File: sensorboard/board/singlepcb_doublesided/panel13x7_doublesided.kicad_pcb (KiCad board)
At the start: 2 copper layers, 200 x 287 mm, 182 parts, among them U0A SiPM, U0B SiPM, U0C SiPM, U0D SiPM, U0E SiPM, U0F SiPM, U0G SiPM, U10A SiPM, U10B SiPM, U10C SiPM, U10D SiPM, U10E SiPM, U10F SiPM, U10G SiPM, U11A SiPM, U11B SiPM, U11C SiPM, U11D SiPM, U11E SiPM, U11F SiPM, U11G SiPM, U12A SiPM, U12B SiPM, U12C SiPM, U12D SiPM, U12E SiPM, U12F SiPM, U12G SiPM, U1A SiPM, U1B SiPM, U1C SiPM, U1D SiPM, U1E SiPM, U1F SiPM, U1G SiPM, U2A SiPM, U2B SiPM, U2C SiPM, U2D SiPM, U2E SiPM, U2F SiPM, U2G SiPM, U3A SiPM, U3B SiPM, U3C SiPM, U3D SiPM, U3E SiPM, U3F SiPM, U3G SiPM, U4A SiPM, U4B SiPM, U4C SiPM, U4D SiPM, U4E SiPM, U4F SiPM, U4G SiPM, U5A SiPM, U5B SiPM, U5C SiPM, U5D SiPM, U5E SiPM, U5F SiPM, U5G SiPM, U6A SiPM, U6B SiPM, U6C SiPM, U6D SiPM, U6E SiPM, U6F SiPM, U6G SiPM, U7A SiPM, U7B SiPM, U7C SiPM, U7D SiPM, U7E SiPM, U7F SiPM, U7G SiPM, U8A SiPM, U8B SiPM, U8C SiPM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

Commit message: Updated 13x7 panel for review.
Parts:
- removed S0A, S0B, S0C, S0D, S0E, S0F: IDC4, idc4:idc4
- removed the S1A at (55.7, 50.7)
- removed U0B, U0C, U0D, U0E, U0F, U0G: SiPM, sipm:sipm
- removed the U1A at (55.6, 29.5)
- added S13A: IDC4, idc4:idc4, B.Cu at (172.3, 50.7)
- added S13B: IDC4, idc4:idc4, B.Cu at (172.3, 81.2)
- added S13C: IDC4, idc4:idc4, B.Cu at (172.3, 111.7)
- added S13D: IDC4, idc4:idc4, B.Cu at (172.3, 142.2)
- added S13E: IDC4, idc4:idc4, B.Cu at (172.3, 172.7)
- added S13F: IDC4, idc4:idc4, B.Cu at (172.3, 203.2)
- added S13G: IDC4, idc4:idc4, B.Cu at (172.3, 233.7)
- added U13A: SiPM, sipm:sipm, F.Cu at (172.2, 29.5)
- added U13B: SiPM, sipm:sipm, F.Cu at (172.2, 60.0)
- added U13C: SiPM, sipm:sipm, F.Cu at (172.2, 90.5)
- added U13D: SiPM, sipm:sipm, F.Cu at (172.2, 121.0)
- added U13E: SiPM, sipm:sipm, F.Cu at (172.2, 151.5)
- added U13F: SiPM, sipm:sipm, F.Cu at (172.2, 182.0)
- added U13G: SiPM, sipm:sipm, F.Cu at (172.2, 212.5)
- moved S4A 10.6 mm to (76.9, 50.7)
- moved S4B 10.6 mm to (76.9, 81.2)
- moved S4C 10.6 mm to (76.9, 111.7)
- moved S4D 10.6 mm to (76.9, 142.2)
- moved S4E 10.6 mm to (76.9, 172.7)
- moved S4F 10.6 mm to (76.9, 203.2)
- moved S4G 10.6 mm to (76.9, 233.7)
- moved S7A 10.6 mm to (108.7, 50.7)
- moved S7B 10.6 mm to (108.7, 81.2)
- moved S7C 10.6 mm to (108.7, 111.7)
- moved S7D 10.6 mm to (108.7, 142.2)
- moved S7E 10.6 mm to (108.7, 172.7)
- moved S7F 10.6 mm to (108.7, 203.2)
- moved S7G 10.6 mm to (108.7, 233.7)
- moved S8A 10.6 mm to (119.3, 50.7)
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- renumbered S0A to S1A, U0A to U1A
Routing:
- net GND: track 0.00 -> 3217.3 mm, vias 91 -> 364
- net Net-(S1-Pad4): track 1839.8 -> 2210.8 mm
- net Net-(S1-Pad3): track 2240.2 -> 2200.7 mm
- net (no net): track 0.60 -> 0.00 mm, vias 91 -> 0
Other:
- outline, holes or cut-outs redrawn
- board text added: "REVIEW VERSION"

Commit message: Left a space between rows, bigger fiducials, larger tabs.
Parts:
- removed S10A, S10B, S10C, S10D, S10E, S10F, S10G, S11A, S11B, S11C, S11D, S11E, S11F, S11G, S12A, S12B, S12C, S12D, S12E, S12F, S12G, S13A, S13B, S13C, S13D, S13E, S13F, S13G, S1B, S1C, S1D, S1E, S1F, S1G, S2A, S2B, S2C, S2D, S2E, S2F, S2G, S3A, S3B, S3C, S3D, S3E, S3F, S3G, S4A, S4B, S4C, S4D, S4E, S4F, S4G, S5A, S5B, S5C, S5D, S5E, S5F, S5G, S6A, S6B, S6C, S6D, S6E, S6F, S6G, S7A, S7B, S7C, S7D, S7E, S7F, S7G, S8A, S8B, S8C, S8D, S8E, S8F, S8G, S9A, S9B, S9C, S9D, S9E, S9F, S9G: IDC4, idc4:idc4
- removed U10A, U10B, U10C, U10D, U10E, U10F, U10G, U11A, U11B, U11C, U11D, U11E, U11F, U11G, U12A, U12B, U12C, U12D, U12E, U12F, U12G, U13A, U13B, U13C, U13D, U13E, U13F, U13G, U1B, U1C, U1D, U1E, U1F, U1G, U2A, U2B, U2C, U2D, U2E, U2F, U2G, U3A, U3B, U3C, U3D, U3E, U3F, U3G, U4A, U4B, U4C, U4D, U4E, U4F, U4G, U5A, U5B, U5C, U5D, U5E, U5F, U5G, U6A, U6B, U6C, U6D, U6E, U6F, U6G, U7A, U7B, U7C, U7D, U7E, U7F, U7G, U8A, U8B, U8C, U8D, U8E, U8F, U8G, U9A, U9B, U9C, U9D, U9E, U9F, U9G: SiPM, sipm:sipm
- added REF**: FID_OxPhys, oxford_fiducial:FID_OxPhys, F.Cu at (20.0, 20.0)
- added REF**: FID_OxPhys, oxford_fiducial:FID_OxPhys, F.Cu at (263.8, 207.0)
- added REF**: FID_OxPhys, oxford_fiducial:FID_OxPhys, F.Cu at (272.0, 228.8)
- added REF**: FID_OxPhys, oxford_fiducial:FID_OxPhys, F.Cu at (294.8, 207.0)
- added REF**: FID_OxPhys, oxford_fiducial:FID_OxPhys, F.Cu at (18.8, 21.0)
- added REF**: FID_OxPhys, oxford_fiducial:FID_OxPhys, F.Cu at (13.2, 260.6)
- added REF**: FID_OxPhys, oxford_fiducial:FID_OxPhys, F.Cu at (188.8, 20.0)
- added REF**: FID_OxPhys, oxford_fiducial:FID_OxPhys, F.Cu at (196.4, 260.6)
- added S101: IDC4, idc4:idc4, B.Cu at (140.5, 50.7)
- added S102: IDC4, idc4:idc4, B.Cu at (140.5, 81.2)
- added S103: IDC4, idc4:idc4, B.Cu at (140.5, 111.7)
- added S104: IDC4, idc4:idc4, B.Cu at (140.5, 142.2)
- added S105: IDC4, idc4:idc4, B.Cu at (140.5, 182.7)
- added S106: IDC4, idc4:idc4, B.Cu at (140.5, 213.2)
- added S107: IDC4, idc4:idc4, B.Cu at (140.5, 243.7)
- added S111: IDC4, idc4:idc4, B.Cu at (151.1, 50.7)
- added S112: IDC4, idc4:idc4, B.Cu at (151.1, 81.2)
- added S113: IDC4, idc4:idc4, B.Cu at (151.1, 111.7)
- added S114: IDC4, idc4:idc4, B.Cu at (151.1, 142.2)
- added S115: IDC4, idc4:idc4, B.Cu at (151.1, 182.7)
- added S116: IDC4, idc4:idc4, B.Cu at (151.1, 213.2)
- added S117: IDC4, idc4:idc4, B.Cu at (151.1, 243.7)
- added S12: IDC4, idc4:idc4, B.Cu at (45.1, 81.2)
- added S121: IDC4, idc4:idc4, B.Cu at (161.7, 50.7)
- added S122: IDC4, idc4:idc4, B.Cu at (161.7, 81.2)
- added S123: IDC4, idc4:idc4, B.Cu at (161.7, 111.7)
- added S124: IDC4, idc4:idc4, B.Cu at (161.7, 142.2)
- added S125: IDC4, idc4:idc4, B.Cu at (161.7, 182.7)
- added S126: IDC4, idc4:idc4, B.Cu at (161.7, 213.2)
- added S127: IDC4, idc4:idc4, B.Cu at (161.7, 243.7)
- added S13: IDC4, idc4:idc4, B.Cu at (45.1, 111.7)
- added S131: IDC4, idc4:idc4, B.Cu at (172.3, 50.7)
- added S132: IDC4, idc4:idc4, B.Cu at (172.3, 81.2)
- added S133: IDC4, idc4:idc4, B.Cu at (172.3, 111.7)
- added S134: IDC4, idc4:idc4, B.Cu at (172.3, 142.2)
- added S135: IDC4, idc4:idc4, B.Cu at (172.3, 182.7)
- added S136: IDC4, idc4:idc4, B.Cu at (172.3, 213.2)
- added S137: IDC4, idc4:idc4, B.Cu at (172.3, 243.7)
- added S14: IDC4, idc4:idc4, B.Cu at (45.1, 142.2)
- added S15: IDC4, idc4:idc4, B.Cu at (45.1, 182.7)
- added S16: IDC4, idc4:idc4, B.Cu at (45.1, 213.2)
- added S17: IDC4, idc4:idc4, B.Cu at (45.1, 243.7)
- added S21: IDC4, idc4:idc4, B.Cu at (55.7, 50.7)
- added S22: IDC4, idc4:idc4, B.Cu at (55.7, 81.2)
- added S23: IDC4, idc4:idc4, B.Cu at (55.7, 111.7)
- added S24: IDC4, idc4:idc4, B.Cu at (55.7, 142.2)
- added S25: IDC4, idc4:idc4, B.Cu at (55.7, 182.7)
- added S26: IDC4, idc4:idc4, B.Cu at (55.7, 213.2)
- added S27: IDC4, idc4:idc4, B.Cu at (55.7, 243.7)
- added S31: IDC4, idc4:idc4, B.Cu at (66.3, 50.7)
- added S32: IDC4, idc4:idc4, B.Cu at (66.3, 81.2)
- added S33: IDC4, idc4:idc4, B.Cu at (66.3, 111.7)
- added S34: IDC4, idc4:idc4, B.Cu at (66.3, 142.2)
- added S35: IDC4, idc4:idc4, B.Cu at (66.3, 182.7)
- added S36: IDC4, idc4:idc4, B.Cu at (66.3, 213.2)
- added S37: IDC4, idc4:idc4, B.Cu at (66.3, 243.7)
- added S41: IDC4, idc4:idc4, B.Cu at (76.9, 50.7)
- added S42: IDC4, idc4:idc4, B.Cu at (76.9, 81.2)
- added S43: IDC4, idc4:idc4, B.Cu at (76.9, 111.7)
- added S44: IDC4, idc4:idc4, B.Cu at (76.9, 142.2)
- added S45: IDC4, idc4:idc4, B.Cu at (76.9, 182.7)
- added S46: IDC4, idc4:idc4, B.Cu at (76.9, 213.2)
- added S47: IDC4, idc4:idc4, B.Cu at (76.9, 243.7)
- added S51: IDC4, idc4:idc4, B.Cu at (87.5, 50.7)
- added S52: IDC4, idc4:idc4, B.Cu at (87.5, 81.2)
- added S53: IDC4, idc4:idc4, B.Cu at (87.5, 111.7)
- added S54: IDC4, idc4:idc4, B.Cu at (87.5, 142.2)
- added S55: IDC4, idc4:idc4, B.Cu at (87.5, 182.7)
- added S56: IDC4, idc4:idc4, B.Cu at (87.5, 213.2)
- added S57: IDC4, idc4:idc4, B.Cu at (87.5, 243.7)
- added S61: IDC4, idc4:idc4, B.Cu at (98.1, 50.7)
- added S62: IDC4, idc4:idc4, B.Cu at (98.1, 81.2)
- added S63: IDC4, idc4:idc4, B.Cu at (98.1, 111.7)
- added S64: IDC4, idc4:idc4, B.Cu at (98.1, 142.2)
- added S65: IDC4, idc4:idc4, B.Cu at (98.1, 182.7)
- added S66: IDC4, idc4:idc4, B.Cu at (98.1, 213.2)
- added S67: IDC4, idc4:idc4, B.Cu at (98.1, 243.7)
- added S71: IDC4, idc4:idc4, B.Cu at (108.7, 50.7)
- added S72: IDC4, idc4:idc4, B.Cu at (108.7, 81.2)
- added S73: IDC4, idc4:idc4, B.Cu at (108.7, 111.7)
- added S74: IDC4, idc4:idc4, B.Cu at (108.7, 142.2)
- added S75: IDC4, idc4:idc4, B.Cu at (108.7, 182.7)
- added S76: IDC4, idc4:idc4, B.Cu at (108.7, 213.2)
- added S77: IDC4, idc4:idc4, B.Cu at (108.7, 243.7)
- added S81: IDC4, idc4:idc4, B.Cu at (119.3, 50.7)
- added S82: IDC4, idc4:idc4, B.Cu at (119.3, 81.2)
- added S83: IDC4, idc4:idc4, B.Cu at (119.3, 111.7)
- added S84: IDC4, idc4:idc4, B.Cu at (119.3, 142.2)
- added S85: IDC4, idc4:idc4, B.Cu at (119.3, 182.7)
- added S86: IDC4, idc4:idc4, B.Cu at (119.3, 213.2)
- added S87: IDC4, idc4:idc4, B.Cu at (119.3, 243.7)
- added S91: IDC4, idc4:idc4, B.Cu at (129.9, 50.7)
- added S92: IDC4, idc4:idc4, B.Cu at (129.9, 81.2)
- added S93: IDC4, idc4:idc4, B.Cu at (129.9, 111.7)
- added S94: IDC4, idc4:idc4, B.Cu at (129.9, 142.2)
- added S95: IDC4, idc4:idc4, B.Cu at (129.9, 182.7)
- added S96: IDC4, idc4:idc4, B.Cu at (129.9, 213.2)
- added S97: IDC4, idc4:idc4, B.Cu at (129.9, 243.7)
- added U101: SiPM, sipm:sipm, F.Cu at (140.4, 29.5)
- added U102: SiPM, sipm:sipm, F.Cu at (140.4, 60.0)
- added U103: SiPM, sipm:sipm, F.Cu at (140.4, 90.5)
- added U104: SiPM, sipm:sipm, F.Cu at (140.4, 121.0)
- added U105: SiPM, sipm:sipm, F.Cu at (140.4, 161.5)
- added U106: SiPM, sipm:sipm, F.Cu at (140.4, 192.0)
- added U107: SiPM, sipm:sipm, F.Cu at (140.4, 222.5)
- added U111: SiPM, sipm:sipm, F.Cu at (151.0, 29.5)
- added U112: SiPM, sipm:sipm, F.Cu at (151.0, 60.0)
- added U113: SiPM, sipm:sipm, F.Cu at (151.0, 90.5)
- added U114: SiPM, sipm:sipm, F.Cu at (151.0, 121.0)
- added U115: SiPM, sipm:sipm, F.Cu at (151.0, 161.5)
- added U116: SiPM, sipm:sipm, F.Cu at (151.0, 192.0)
- added U117: SiPM, sipm:sipm, F.Cu at (151.0, 222.5)
- added U12: SiPM, sipm:sipm, F.Cu at (45.0, 60.0)
- added U121: SiPM, sipm:sipm, F.Cu at (161.6, 29.5)
- added U122: SiPM, sipm:sipm, F.Cu at (161.6, 60.0)
- added U123: SiPM, sipm:sipm, F.Cu at (161.6, 90.5)
- added U124: SiPM, sipm:sipm, F.Cu at (161.6, 121.0)
- added U125: SiPM, sipm:sipm, F.Cu at (161.6, 161.5)
- added U126: SiPM, sipm:sipm, F.Cu at (161.6, 192.0)
- added U127: SiPM, sipm:sipm, F.Cu at (161.6, 222.5)
- added U13: SiPM, sipm:sipm, F.Cu at (45.0, 90.5)
- added U131: SiPM, sipm:sipm, F.Cu at (172.2, 29.5)
- added U132: SiPM, sipm:sipm, F.Cu at (172.2, 60.0)
- added U133: SiPM, sipm:sipm, F.Cu at (172.2, 90.5)
- added U134: SiPM, sipm:sipm, F.Cu at (172.2, 121.0)
- added U135: SiPM, sipm:sipm, F.Cu at (172.2, 161.5)
- added U136: SiPM, sipm:sipm, F.Cu at (172.2, 192.0)
- added U137: SiPM, sipm:sipm, F.Cu at (172.2, 222.5)
- added U14: SiPM, sipm:sipm, F.Cu at (45.0, 121.0)
- added U15: SiPM, sipm:sipm, F.Cu at (45.0, 161.5)
- added U16: SiPM, sipm:sipm, F.Cu at (45.0, 192.0)
- added U17: SiPM, sipm:sipm, F.Cu at (45.0, 222.5)
- added U21: SiPM, sipm:sipm, F.Cu at (55.6, 29.5)
- added U22: SiPM, sipm:sipm, F.Cu at (55.6, 60.0)
- added U23: SiPM, sipm:sipm, F.Cu at (55.6, 90.5)
- added U24: SiPM, sipm:sipm, F.Cu at (55.6, 121.0)
- added U25: SiPM, sipm:sipm, F.Cu at (55.6, 161.5)
- added U26: SiPM, sipm:sipm, F.Cu at (55.6, 192.0)
- added U27: SiPM, sipm:sipm, F.Cu at (55.6, 222.5)
- added U31: SiPM, sipm:sipm, F.Cu at (66.2, 29.5)
- added U32: SiPM, sipm:sipm, F.Cu at (66.2, 60.0)
- added U33: SiPM, sipm:sipm, F.Cu at (66.2, 90.5)
- added U34: SiPM, sipm:sipm, F.Cu at (66.2, 121.0)
- added U35: SiPM, sipm:sipm, F.Cu at (66.2, 161.5)
- added U36: SiPM, sipm:sipm, F.Cu at (66.2, 192.0)
- added U37: SiPM, sipm:sipm, F.Cu at (66.2, 222.5)
- added U41: SiPM, sipm:sipm, F.Cu at (76.8, 29.5)
- added U42: SiPM, sipm:sipm, F.Cu at (76.8, 60.0)
- added U43: SiPM, sipm:sipm, F.Cu at (76.8, 90.5)
- added U44: SiPM, sipm:sipm, F.Cu at (76.8, 121.0)
- added U45: SiPM, sipm:sipm, F.Cu at (76.8, 161.5)
- added U46: SiPM, sipm:sipm, F.Cu at (76.8, 192.0)
- added U47: SiPM, sipm:sipm, F.Cu at (76.8, 222.5)
- added U51: SiPM, sipm:sipm, F.Cu at (87.4, 29.5)
- added U52: SiPM, sipm:sipm, F.Cu at (87.4, 60.0)
- added U53: SiPM, sipm:sipm, F.Cu at (87.4, 90.5)
- added U54: SiPM, sipm:sipm, F.Cu at (87.4, 121.0)
- added U55: SiPM, sipm:sipm, F.Cu at (87.4, 161.5)
- added U56: SiPM, sipm:sipm, F.Cu at (87.4, 192.0)
- added U57: SiPM, sipm:sipm, F.Cu at (87.4, 222.5)
- added U61: SiPM, sipm:sipm, F.Cu at (98.0, 29.5)
- added U62: SiPM, sipm:sipm, F.Cu at (98.0, 60.0)
- added U63: SiPM, sipm:sipm, F.Cu at (98.0, 90.5)
- added U64: SiPM, sipm:sipm, F.Cu at (98.0, 121.0)
- added U65: SiPM, sipm:sipm, F.Cu at (98.0, 161.5)
- added U66: SiPM, sipm:sipm, F.Cu at (98.0, 192.0)
- added U67: SiPM, sipm:sipm, F.Cu at (98.0, 222.5)
- added U71: SiPM, sipm:sipm, F.Cu at (108.6, 29.5)
- added U72: SiPM, sipm:sipm, F.Cu at (108.6, 60.0)
- added U73: SiPM, sipm:sipm, F.Cu at (108.6, 90.5)
- added U74: SiPM, sipm:sipm, F.Cu at (108.6, 121.0)
- added U75: SiPM, sipm:sipm, F.Cu at (108.6, 161.5)
- added U76: SiPM, sipm:sipm, F.Cu at (108.6, 192.0)
- added U77: SiPM, sipm:sipm, F.Cu at (108.6, 222.5)
- added U81: SiPM, sipm:sipm, F.Cu at (119.2, 29.5)
- added U82: SiPM, sipm:sipm, F.Cu at (119.2, 60.0)
- added U83: SiPM, sipm:sipm, F.Cu at (119.2, 90.5)
- added U84: SiPM, sipm:sipm, F.Cu at (119.2, 121.0)
- added U85: SiPM, sipm:sipm, F.Cu at (119.2, 161.5)
- added U86: SiPM, sipm:sipm, F.Cu at (119.2, 192.0)
- added U87: SiPM, sipm:sipm, F.Cu at (119.2, 222.5)
- added U91: SiPM, sipm:sipm, F.Cu at (129.8, 29.5)
- added U92: SiPM, sipm:sipm, F.Cu at (129.8, 60.0)
- added U93: SiPM, sipm:sipm, F.Cu at (129.8, 90.5)
- added U94: SiPM, sipm:sipm, F.Cu at (129.8, 121.0)
- added U95: SiPM, sipm:sipm, F.Cu at (129.8, 161.5)
- added U96: SiPM, sipm:sipm, F.Cu at (129.8, 192.0)
- added U97: SiPM, sipm:sipm, F.Cu at (129.8, 222.5)
- renumbered S1A to S11, U1A to U11
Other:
- board size 200 x 287 mm -> 200 x 262.1 mm
- board text added: "SoLid SiPM sensor boards. 22 Jun 16. Nick Ryder nick.ryder@physics.ox.ac.uk"
- board text removed: "REVIEW VERSION"
- board text removed: "SoLid SiPM sensor boards. 13 Jun 16. Nick Ryder nick.ryder@physics.ox.ac.uk"

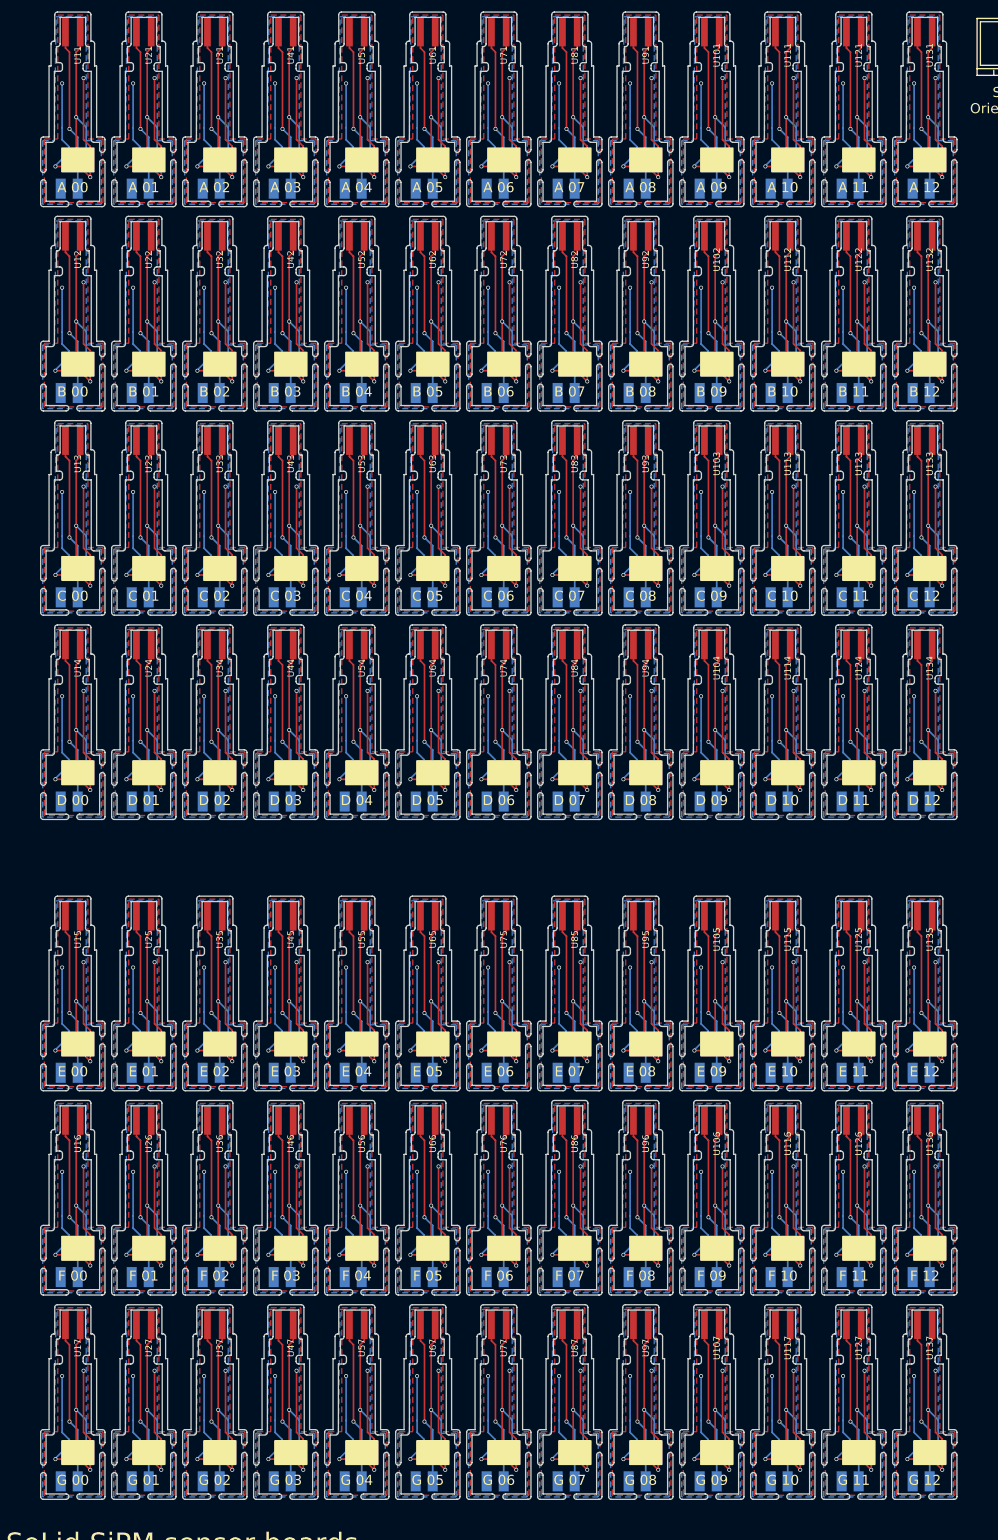
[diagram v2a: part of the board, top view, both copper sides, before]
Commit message: Working on MPPC PCB cut outs.
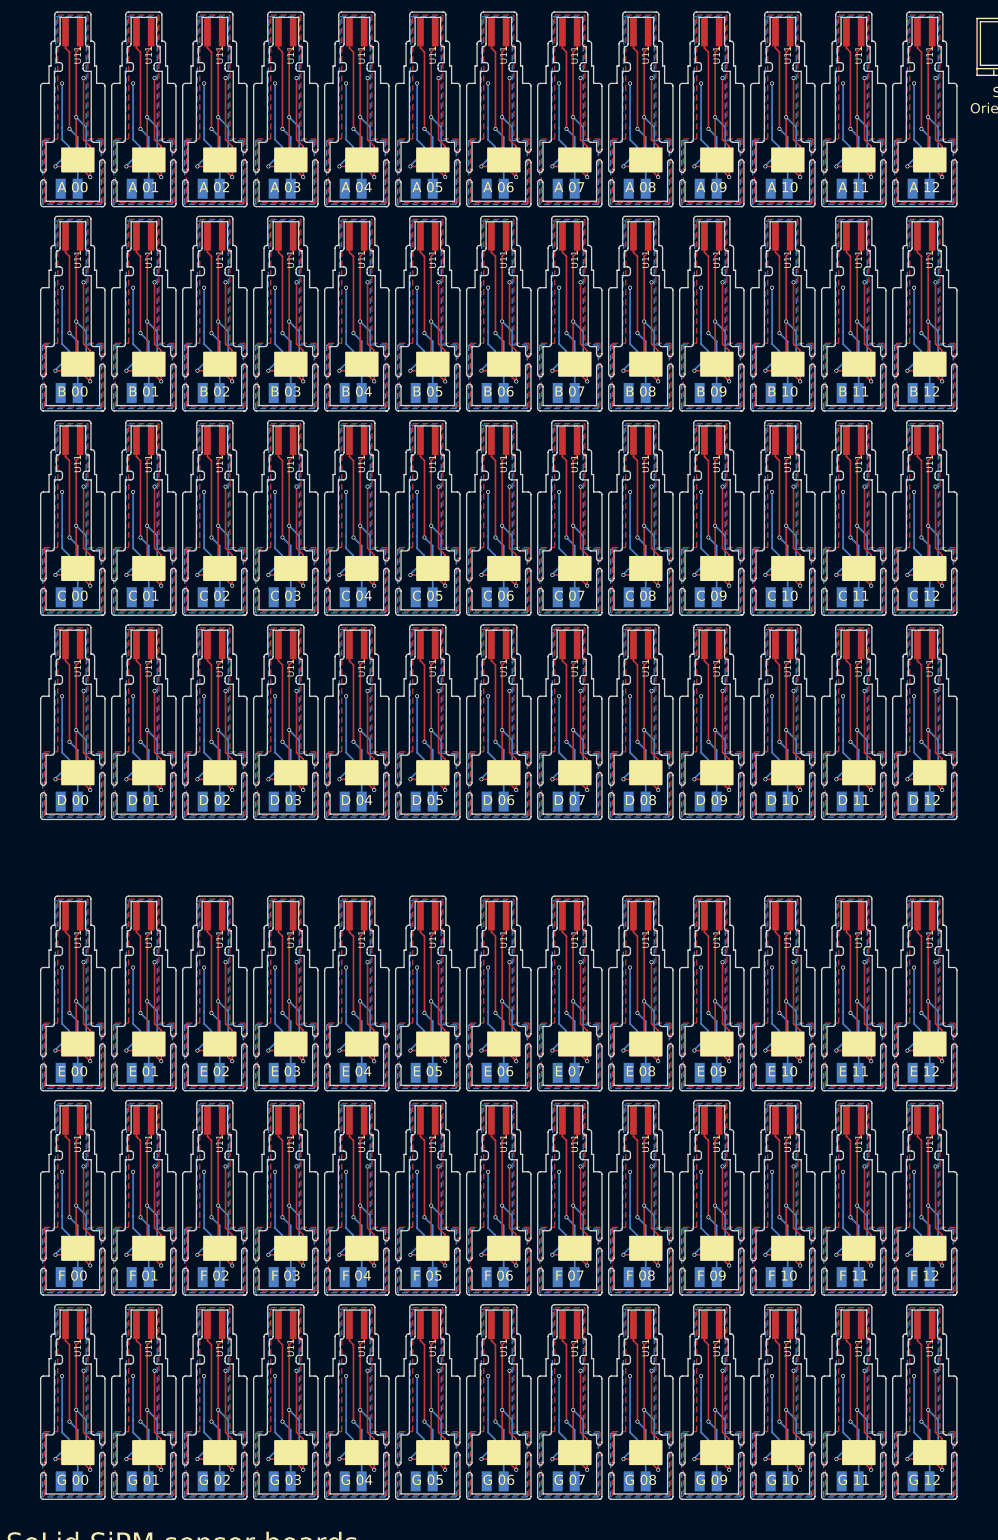
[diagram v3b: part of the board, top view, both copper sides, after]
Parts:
- removed S101, S102, S103, S104, S105, S106, S107, S111, S112, S113, S114, S115, S116, S117, S12, S121, S122, S123, S124, S125, S126, S127, S13, S131, S132, S133, S134, S135, S136, S137, S14, S15, S16, S17, S21, S22, S23, S24, S25, S26, S27, S31, S32, S33, S34, S35, S36, S37, S41, S42, S43, S44, S45, S46, S47, S51, S52, S53, S54, S55, S56, S57, S61, S62, S63, S64, S65, S66, S67, S71, S72, S73, S74, S75, S76, S77, S81, S82, S83, S84, S85, S86, S87, S91, S92, S93, S94, S95, S96, S97: IDC4, idc4:idc4
- removed U101, U102, U103, U104, U105, U106, U107, U111, U112, U113, U114, U115, U116, U117, U12, U121, U122, U123, U124, U125, U126, U127, U13, U131, U132, U133, U134, U135, U136, U137, U14, U15, U16, U17, U21, U22, U23, U24, U25, U26, U27, U31, U32, U33, U34, U35, U36, U37, U41, U42, U43, U44, U45, U46, U47, U51, U52, U53, U54, U55, U56, U57, U61, U62, U63, U64, U65, U66, U67, U71, U72, U73, U74, U75, U76, U77, U81, U82, U83, U84, U85, U86, U87, U91, U92, U93, U94, U95, U96, U97: SiPM, sipm:sipm
- added S11: IDC4, idc4:idc4, B.Cu at (87.5, 243.7)
- added S11: IDC4, idc4:idc4, B.Cu at (76.9, 213.2)
- added S11: IDC4, idc4:idc4, B.Cu at (108.7, 243.7)
- added S11: IDC4, idc4:idc4, B.Cu at (108.7, 213.2)
- added S11: IDC4, idc4:idc4, B.Cu at (98.1, 243.7)
- added S11: IDC4, idc4:idc4, B.Cu at (98.1, 213.2)
- added S11: IDC4, idc4:idc4, B.Cu at (172.3, 243.7)
- added S11: IDC4, idc4:idc4, B.Cu at (172.3, 213.2)
- added S11: IDC4, idc4:idc4, B.Cu at (119.3, 243.7)
- added S11: IDC4, idc4:idc4, B.Cu at (119.3, 213.2)
- added S11: IDC4, idc4:idc4, B.Cu at (151.1, 243.7)
- added S11: IDC4, idc4:idc4, B.Cu at (87.5, 213.2)
- added S11: IDC4, idc4:idc4, B.Cu at (151.1, 213.2)
- added S11: IDC4, idc4:idc4, B.Cu at (129.9, 243.7)
- added S11: IDC4, idc4:idc4, B.Cu at (129.9, 213.2)
- added S11: IDC4, idc4:idc4, B.Cu at (140.5, 243.7)
- added S11: IDC4, idc4:idc4, B.Cu at (140.5, 213.2)
- added S11: IDC4, idc4:idc4, B.Cu at (161.7, 243.7)
- added S11: IDC4, idc4:idc4, B.Cu at (161.7, 213.2)
- added S11: IDC4, idc4:idc4, B.Cu at (172.3, 182.7)
- added S11: IDC4, idc4:idc4, B.Cu at (161.7, 182.7)
- added S11: IDC4, idc4:idc4, B.Cu at (119.3, 182.7)
- added S11: IDC4, idc4:idc4, B.Cu at (66.3, 243.7)
- added S11: IDC4, idc4:idc4, B.Cu at (151.1, 182.7)
- added S11: IDC4, idc4:idc4, B.Cu at (129.9, 182.7)
- added S11: IDC4, idc4:idc4, B.Cu at (140.5, 182.7)
- added S11: IDC4, idc4:idc4, B.Cu at (108.7, 182.7)
- added S11: IDC4, idc4:idc4, B.Cu at (98.1, 182.7)
- added S11: IDC4, idc4:idc4, B.Cu at (87.5, 182.7)
- added S11: IDC4, idc4:idc4, B.Cu at (66.3, 182.7)
- added S11: IDC4, idc4:idc4, B.Cu at (55.7, 182.7)
- added S11: IDC4, idc4:idc4, B.Cu at (45.1, 182.7)
- added S11: IDC4, idc4:idc4, B.Cu at (76.9, 182.7)
- added S11: IDC4, idc4:idc4, B.Cu at (66.3, 213.2)
- added S11: IDC4, idc4:idc4, B.Cu at (119.3, 142.2)
- added S11: IDC4, idc4:idc4, B.Cu at (119.3, 111.7)
- added S11: IDC4, idc4:idc4, B.Cu at (119.3, 81.2)
- added S11: IDC4, idc4:idc4, B.Cu at (108.7, 142.2)
- added S11: IDC4, idc4:idc4, B.Cu at (108.7, 111.7)
- added S11: IDC4, idc4:idc4, B.Cu at (108.7, 81.2)
- added S11: IDC4, idc4:idc4, B.Cu at (98.1, 142.2)
- added S11: IDC4, idc4:idc4, B.Cu at (98.1, 111.7)
- added S11: IDC4, idc4:idc4, B.Cu at (98.1, 81.2)
- added S11: IDC4, idc4:idc4, B.Cu at (87.5, 142.2)
- added S11: IDC4, idc4:idc4, B.Cu at (55.7, 243.7)
- added S11: IDC4, idc4:idc4, B.Cu at (87.5, 111.7)
- added S11: IDC4, idc4:idc4, B.Cu at (87.5, 81.2)
- added S11: IDC4, idc4:idc4, B.Cu at (172.3, 142.2)
- added S11: IDC4, idc4:idc4, B.Cu at (172.3, 111.7)
- added S11: IDC4, idc4:idc4, B.Cu at (172.3, 81.2)
- added S11: IDC4, idc4:idc4, B.Cu at (140.5, 142.2)
- added S11: IDC4, idc4:idc4, B.Cu at (140.5, 111.7)
- added S11: IDC4, idc4:idc4, B.Cu at (140.5, 81.2)
- added S11: IDC4, idc4:idc4, B.Cu at (129.9, 142.2)
- added S11: IDC4, idc4:idc4, B.Cu at (129.9, 111.7)
- added S11: IDC4, idc4:idc4, B.Cu at (55.7, 213.2)
- added S11: IDC4, idc4:idc4, B.Cu at (129.9, 81.2)
- added S11: IDC4, idc4:idc4, B.Cu at (151.1, 142.2)
- added S11: IDC4, idc4:idc4, B.Cu at (151.1, 111.7)
- added S11: IDC4, idc4:idc4, B.Cu at (151.1, 81.2)
- added S11: IDC4, idc4:idc4, B.Cu at (161.7, 142.2)
- added S11: IDC4, idc4:idc4, B.Cu at (161.7, 111.7)
- added S11: IDC4, idc4:idc4, B.Cu at (161.7, 81.2)
- added S11: IDC4, idc4:idc4, B.Cu at (66.3, 142.2)
- added S11: IDC4, idc4:idc4, B.Cu at (66.3, 111.7)
- added S11: IDC4, idc4:idc4, B.Cu at (66.3, 81.2)
- added S11: IDC4, idc4:idc4, B.Cu at (45.1, 243.7)
- added S11: IDC4, idc4:idc4, B.Cu at (55.7, 142.2)
- added S11: IDC4, idc4:idc4, B.Cu at (55.7, 111.7)
- added S11: IDC4, idc4:idc4, B.Cu at (55.7, 81.2)
- added S11: IDC4, idc4:idc4, B.Cu at (45.1, 142.2)
- added S11: IDC4, idc4:idc4, B.Cu at (45.1, 111.7)
- added S11: IDC4, idc4:idc4, B.Cu at (45.1, 81.2)
- added S11: IDC4, idc4:idc4, B.Cu at (76.9, 142.2)
- added S11: IDC4, idc4:idc4, B.Cu at (76.9, 111.7)
- added S11: IDC4, idc4:idc4, B.Cu at (76.9, 81.2)
- added S11: IDC4, idc4:idc4, B.Cu at (172.3, 50.7)
- added S11: IDC4, idc4:idc4, B.Cu at (45.1, 213.2)
- added S11: IDC4, idc4:idc4, B.Cu at (161.7, 50.7)
- added S11: IDC4, idc4:idc4, B.Cu at (151.1, 50.7)
- added S11: IDC4, idc4:idc4, B.Cu at (140.5, 50.7)
- added S11: IDC4, idc4:idc4, B.Cu at (129.9, 50.7)
- added S11: IDC4, idc4:idc4, B.Cu at (119.3, 50.7)
- added S11: IDC4, idc4:idc4, B.Cu at (108.7, 50.7)
- added S11: IDC4, idc4:idc4, B.Cu at (98.1, 50.7)
- added S11: IDC4, idc4:idc4, B.Cu at (87.5, 50.7)
- added S11: IDC4, idc4:idc4, B.Cu at (76.9, 50.7)
- added S11: IDC4, idc4:idc4, B.Cu at (66.3, 50.7)
- added S11: IDC4, idc4:idc4, B.Cu at (76.9, 243.7)
- added S11: IDC4, idc4:idc4, B.Cu at (55.7, 50.7)
- added U11: SiPM, sipm:sipm, F.Cu at (76.8, 222.5)
- added U11: SiPM, sipm:sipm, F.Cu at (108.6, 192.0)
- added U11: SiPM, sipm:sipm, F.Cu at (119.2, 222.5)
- added U11: SiPM, sipm:sipm, F.Cu at (119.2, 192.0)
- added U11: SiPM, sipm:sipm, F.Cu at (98.0, 222.5)
- added U11: SiPM, sipm:sipm, F.Cu at (98.0, 192.0)
- added U11: SiPM, sipm:sipm, F.Cu at (87.4, 222.5)
- added U11: SiPM, sipm:sipm, F.Cu at (87.4, 192.0)
- added U11: SiPM, sipm:sipm, F.Cu at (151.0, 222.5)
- added U11: SiPM, sipm:sipm, F.Cu at (151.0, 192.0)
- added U11: SiPM, sipm:sipm, F.Cu at (140.4, 222.5)
- added U11: SiPM, sipm:sipm, F.Cu at (76.8, 192.0)
- added U11: SiPM, sipm:sipm, F.Cu at (140.4, 192.0)
- added U11: SiPM, sipm:sipm, F.Cu at (129.8, 222.5)
- added U11: SiPM, sipm:sipm, F.Cu at (129.8, 192.0)
- added U11: SiPM, sipm:sipm, F.Cu at (161.6, 222.5)
- added U11: SiPM, sipm:sipm, F.Cu at (161.6, 192.0)
- added U11: SiPM, sipm:sipm, F.Cu at (172.2, 222.5)
- added U11: SiPM, sipm:sipm, F.Cu at (172.2, 192.0)
- added U11: SiPM, sipm:sipm, F.Cu at (129.8, 161.5)
- added U11: SiPM, sipm:sipm, F.Cu at (161.6, 161.5)
- added U11: SiPM, sipm:sipm, F.Cu at (151.0, 161.5)
- added U11: SiPM, sipm:sipm, F.Cu at (66.2, 222.5)
- added U11: SiPM, sipm:sipm, F.Cu at (140.4, 161.5)
- added U11: SiPM, sipm:sipm, F.Cu at (172.2, 161.5)
- added U11: SiPM, sipm:sipm, F.Cu at (76.8, 161.5)
- added U11: SiPM, sipm:sipm, F.Cu at (119.2, 161.5)
- added U11: SiPM, sipm:sipm, F.Cu at (98.0, 161.5)
- added U11: SiPM, sipm:sipm, F.Cu at (108.6, 161.5)
- added U11: SiPM, sipm:sipm, F.Cu at (66.2, 161.5)
- added U11: SiPM, sipm:sipm, F.Cu at (87.4, 161.5)
- added U11: SiPM, sipm:sipm, F.Cu at (45.0, 161.5)
- added U11: SiPM, sipm:sipm, F.Cu at (55.6, 161.5)
- added U11: SiPM, sipm:sipm, F.Cu at (66.2, 192.0)
- added U11: SiPM, sipm:sipm, F.Cu at (76.8, 121.0)
- added U11: SiPM, sipm:sipm, F.Cu at (76.8, 90.5)
- added U11: SiPM, sipm:sipm, F.Cu at (76.8, 60.0)
- added U11: SiPM, sipm:sipm, F.Cu at (87.4, 121.0)
- added U11: SiPM, sipm:sipm, F.Cu at (87.4, 90.5)
- added U11: SiPM, sipm:sipm, F.Cu at (87.4, 60.0)
- added U11: SiPM, sipm:sipm, F.Cu at (98.0, 121.0)
- added U11: SiPM, sipm:sipm, F.Cu at (98.0, 90.5)
- added U11: SiPM, sipm:sipm, F.Cu at (98.0, 60.0)
- added U11: SiPM, sipm:sipm, F.Cu at (129.8, 121.0)
- added U11: SiPM, sipm:sipm, F.Cu at (45.0, 222.5)
- added U11: SiPM, sipm:sipm, F.Cu at (129.8, 90.5)
- added U11: SiPM, sipm:sipm, F.Cu at (129.8, 60.0)
- added U11: SiPM, sipm:sipm, F.Cu at (119.2, 121.0)
- added U11: SiPM, sipm:sipm, F.Cu at (119.2, 90.5)
- added U11: SiPM, sipm:sipm, F.Cu at (119.2, 60.0)
- added U11: SiPM, sipm:sipm, F.Cu at (108.6, 121.0)
- added U11: SiPM, sipm:sipm, F.Cu at (108.6, 90.5)
- added U11: SiPM, sipm:sipm, F.Cu at (108.6, 60.0)
- added U11: SiPM, sipm:sipm, F.Cu at (66.2, 121.0)
- added U11: SiPM, sipm:sipm, F.Cu at (66.2, 90.5)
- added U11: SiPM, sipm:sipm, F.Cu at (45.0, 192.0)
- added U11: SiPM, sipm:sipm, F.Cu at (66.2, 60.0)
- added U11: SiPM, sipm:sipm, F.Cu at (45.0, 121.0)
- added U11: SiPM, sipm:sipm, F.Cu at (45.0, 90.5)
- added U11: SiPM, sipm:sipm, F.Cu at (45.0, 60.0)
- added U11: SiPM, sipm:sipm, F.Cu at (55.6, 121.0)
- added U11: SiPM, sipm:sipm, F.Cu at (55.6, 90.5)
- added U11: SiPM, sipm:sipm, F.Cu at (55.6, 60.0)
- added U11: SiPM, sipm:sipm, F.Cu at (161.6, 121.0)
- added U11: SiPM, sipm:sipm, F.Cu at (161.6, 90.5)
- added U11: SiPM, sipm:sipm, F.Cu at (161.6, 60.0)
- added U11: SiPM, sipm:sipm, F.Cu at (55.6, 222.5)
- added U11: SiPM, sipm:sipm, F.Cu at (140.4, 121.0)
- added U11: SiPM, sipm:sipm, F.Cu at (140.4, 90.5)
- added U11: SiPM, sipm:sipm, F.Cu at (140.4, 60.0)
- added U11: SiPM, sipm:sipm, F.Cu at (151.0, 121.0)
- added U11: SiPM, sipm:sipm, F.Cu at (151.0, 90.5)
- added U11: SiPM, sipm:sipm, F.Cu at (151.0, 60.0)
- added U11: SiPM, sipm:sipm, F.Cu at (172.2, 121.0)
- added U11: SiPM, sipm:sipm, F.Cu at (172.2, 90.5)
- added U11: SiPM, sipm:sipm, F.Cu at (172.2, 60.0)
- added U11: SiPM, sipm:sipm, F.Cu at (172.2, 29.5)
- added U11: SiPM, sipm:sipm, F.Cu at (55.6, 192.0)
- added U11: SiPM, sipm:sipm, F.Cu at (161.6, 29.5)
- added U11: SiPM, sipm:sipm, F.Cu at (151.0, 29.5)
- added U11: SiPM, sipm:sipm, F.Cu at (140.4, 29.5)
- added U11: SiPM, sipm:sipm, F.Cu at (129.8, 29.5)
- added U11: SiPM, sipm:sipm, F.Cu at (119.2, 29.5)
- added U11: SiPM, sipm:sipm, F.Cu at (108.6, 29.5)
- added U11: SiPM, sipm:sipm, F.Cu at (98.0, 29.5)
- added U11: SiPM, sipm:sipm, F.Cu at (87.4, 29.5)
- added U11: SiPM, sipm:sipm, F.Cu at (76.8, 29.5)
- added U11: SiPM, sipm:sipm, F.Cu at (66.2, 29.5)
- added U11: SiPM, sipm:sipm, F.Cu at (108.6, 222.5)
- added U11: SiPM, sipm:sipm, F.Cu at (55.6, 29.5)
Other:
- outline, holes or cut-outs redrawn
